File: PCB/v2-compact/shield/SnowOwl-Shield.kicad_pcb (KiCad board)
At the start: 4 copper layers, 60 x 85 mm, 1 part, among them J1 STACK_2x10

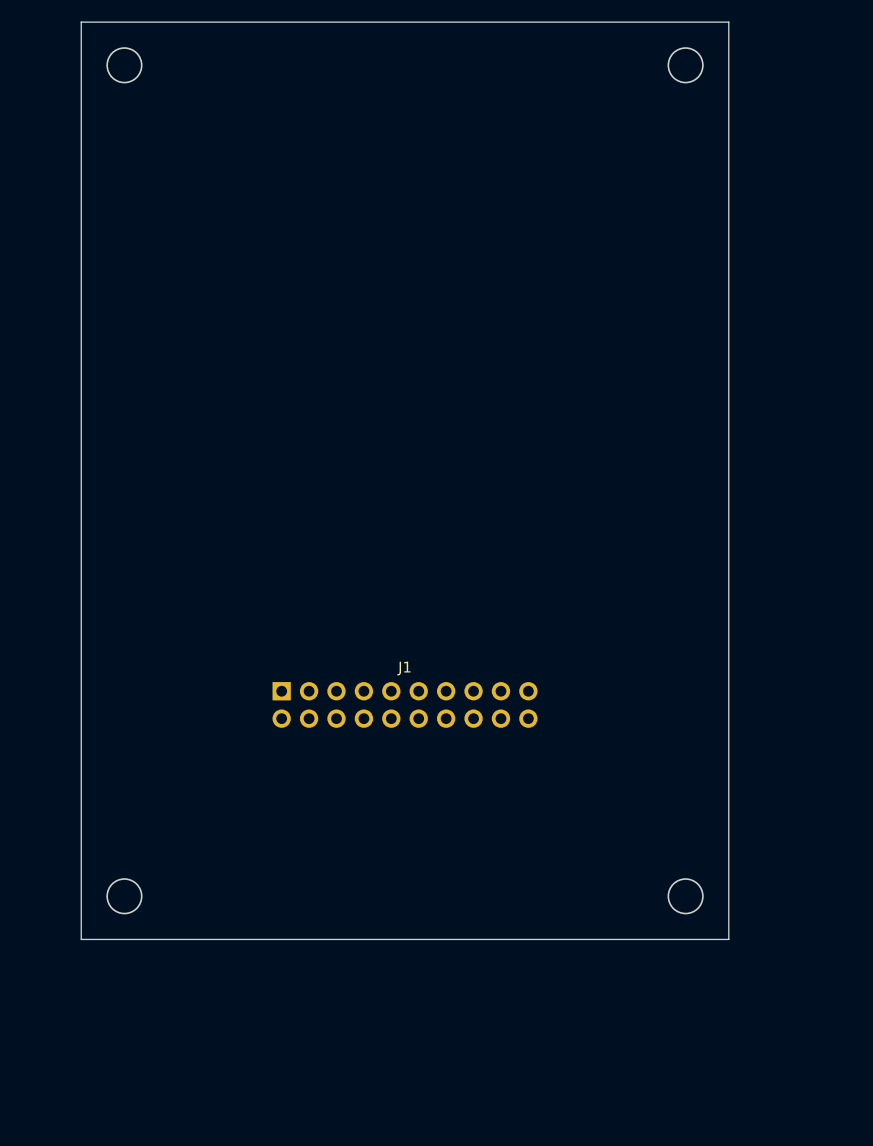
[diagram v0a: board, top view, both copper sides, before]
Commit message: PCB v2: grow to 70x100mm and adopt the C5-owns-radios architecture
Refit the outline to 70x100 after a footprint fit-check: 60x85 could not hold
the RV1106 SoM plus the C5 and nRF24 modules without cramming, which is what
forces congested traces.

- ESP32-C5 now masters the shield SPI spine; every SPI radio taps off it, so
  the whole radio fan-out stays on the shield next to the C5. The S3 commands
  the C5 over one UART on J1 and no SPI radio line crosses the stack header.
- Reflow both boards' zones for short-trace placement, sized to the real part
  footprints; keep the shared J1 datum (53.57, 106.0) so the boards still stack.
- Lock the J1 pinout: power + I2C(PN532) + S3<->C5 UART + S3<->RV1106 UART +
  IR + 1-Wire, with grounds spread for clean returns.
- Rewrite PLACEMENT.md as the updated contract; refresh the shield schematic
  intent note and both floorplan SVGs.
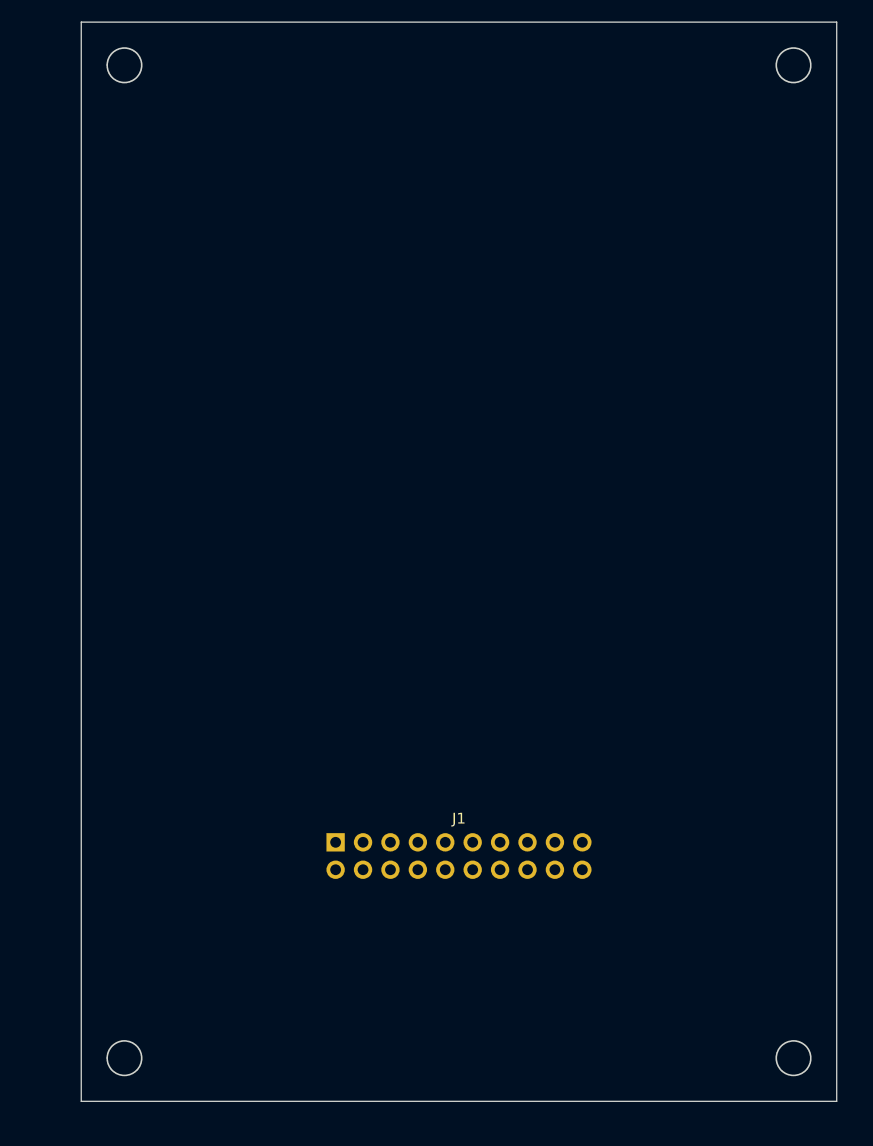
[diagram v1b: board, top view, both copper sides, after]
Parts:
- moved J1 14.9 mm to (53.6, 106.0)
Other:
- board size 60 x 85 mm -> 70 x 100 mm
- board text added: "(BACK) HTRC110 125k + coil"
- board text added: "< LF coil 125k"
- board text added: "< NFC coil 13.56M"
- board text added: "ESP32-C5 (SPI MASTER)"
- board text added: "FRONT=User.1 BACK=User.2 C5 masters shield SPI spine; J1 = power + S3/RV1106 links"
- board text added: "RV1106 USB-C + uSD >"
- board text removed: "(BACK) HTRC110 125kHz + coil"
- board text removed: "< LF coil"
- board text removed: "< NFC coil"
- board text removed: "ESP32-C5 + LDO (U.FL)"
- board text removed: "FRONT zones = User.1 BACK zones = User.2 (floorplan skeleton)"
- board text removed: "RV1106 USB-C >"

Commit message: PCB: import schematic netlists onto both boards (parts placed + nets assigned)
Load every footprint from the schematic into the floorplan-skeleton boards,
place each in its subsystem's zone (grid-spread, back-side sheets flipped), and
assign all nets. Shield: 79 parts, 419 pad-nets, 153 nets. Main: 29 parts,
150 pad-nets, 57 nets. Register the Espressif footprint library; add a
placeholder Core1106 SoM footprint; assign the C5 (Espressif), NEO-M9N (ublox_NEO)
and CC1101 (2x4 header) module footprints.

This is the initial import: every part is on its board with the full ratsnest,
ready for placement refinement and routing.
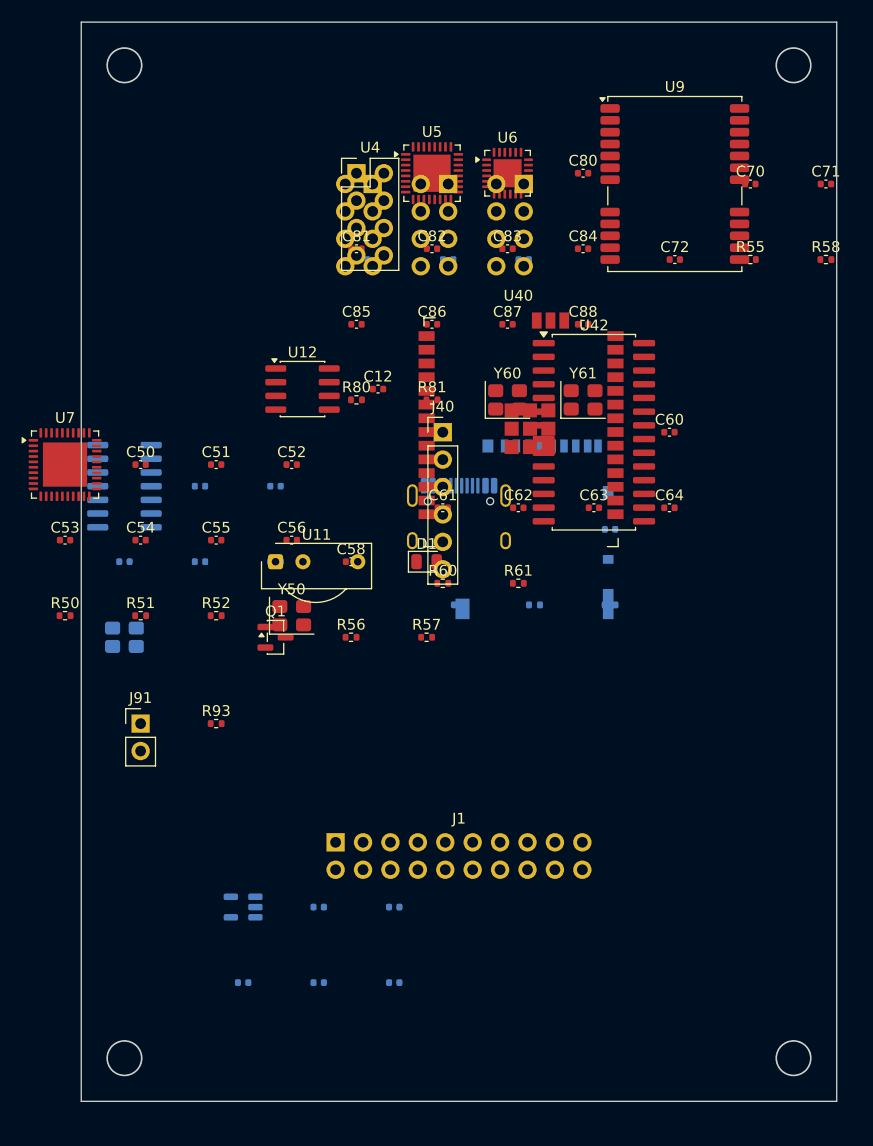
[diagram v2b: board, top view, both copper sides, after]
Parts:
- added C10: 100nF, C_0402_1005Metric, B.Cu at (57.0, 52.0)
- added C12: 100nF, C_0402_1005Metric, F.Cu at (57.5, 64.0)
- added C20: 100nF, C_0402_1005Metric, B.Cu at (64.0, 52.0)
- added C30: 100nF, C_0402_1005Metric, B.Cu at (71.0, 52.0)
- added C40: 10uF, C_0402_1005Metric, B.Cu at (52.0, 112.0)
- added C41: 10uF, C_0402_1005Metric, B.Cu at (59.0, 112.0)
- added C42: 100nF, C_0402_1005Metric, B.Cu at (45.0, 119.0)
- added C43: 22uF, C_0402_1005Metric, B.Cu at (52.0, 119.0)
- added C44: 22uF, C_0402_1005Metric, B.Cu at (59.0, 119.0)
- added C50: 18pF, C_0402_1005Metric, F.Cu at (35.5, 71.0)
- added C51: 18pF, C_0402_1005Metric, F.Cu at (42.5, 71.0)
- added C52: 100nF, C_0402_1005Metric, F.Cu at (49.5, 71.0)
- added C53: 100nF, C_0402_1005Metric, F.Cu at (28.5, 78.0)
- added C54: 1uF, C_0402_1005Metric, F.Cu at (35.5, 78.0)
- added C55: 100nF, C_0402_1005Metric, F.Cu at (42.5, 78.0)
- added C56: 100nF, C_0402_1005Metric, F.Cu at (49.5, 78.0)
- added C58: 100nF, C_0402_1005Metric, F.Cu at (55.0, 80.0)
- added C60: 10uF, C_0402_1005Metric, F.Cu at (84.5, 68.0)
- added C61: 100nF, C_0402_1005Metric, F.Cu at (63.5, 75.0)
- added C62: 100nF, C_0402_1005Metric, F.Cu at (70.5, 75.0)
- added C63: 1uF, C_0402_1005Metric, F.Cu at (77.5, 75.0)
- added C64: 100nF, C_0402_1005Metric, F.Cu at (84.5, 75.0)
- added C70: 100nF, C_0402_1005Metric, F.Cu at (92.0, 45.0)
- added C71: 10uF, C_0402_1005Metric, F.Cu at (99.0, 45.0)
- added C72: 1uF, C_0402_1005Metric, F.Cu at (85.0, 52.0)
- added C80: 10pF, C_0402_1005Metric, F.Cu at (76.5, 44.0)
- added C81: 10pF, C_0402_1005Metric, F.Cu at (55.5, 51.0)
- added C82: 100nF, C_0402_1005Metric, F.Cu at (62.5, 51.0)
- added C83: 100nF, C_0402_1005Metric, F.Cu at (69.5, 51.0)
- added C84: 12pF, C_0402_1005Metric, F.Cu at (76.5, 51.0)
- added C85: 12pF, C_0402_1005Metric, F.Cu at (55.5, 58.0)
- added C86: 100nF, C_0402_1005Metric, F.Cu at (62.5, 58.0)
- added C87: 100nF, C_0402_1005Metric, F.Cu at (69.5, 58.0)
- added C88: 100nF, C_0402_1005Metric, F.Cu at (76.5, 58.0)
- added C90: 18pF, C_0402_1005Metric, B.Cu at (41.0, 73.0)
- added C91: 18pF, C_0402_1005Metric, B.Cu at (48.0, 73.0)
- added C92: 100nF, C_0402_1005Metric, B.Cu at (34.0, 80.0)
- added C93: 10uF, C_0402_1005Metric, B.Cu at (41.0, 80.0)
- added C94: 10uF, C_0402_1005Metric, B.Cu at (79.0, 77.0)
- added C95: 10uF, C_0402_1005Metric, B.Cu at (65.0, 84.0)
- added D1: IR_LED, LED_0805_2012Metric, F.Cu at (62.0, 80.0)
- added J40: C5_PROG_UART, PinHeader_1x06_P2.54mm_Vertical, F.Cu at (63.5, 68.0)
- added J50: USB-C, USB_C_Receptacle_HRO_TYPE-C-31-M-12, B.Cu at (65.0, 77.0)
- added J51: microSD, microSD_HC_Hirose_DM3AT-SF-PEJM5, B.Cu at (72.0, 77.0)
- added J91: iButton, PinHeader_1x02_P2.54mm_Vertical, F.Cu at (35.5, 95.0)
- added Q1: MMBT3904, SOT-23, F.Cu at (48.0, 87.0)
- added R50: 4k7, R_0402_1005Metric, F.Cu at (28.5, 85.0)
- added R51: 4k7, R_0402_1005Metric, F.Cu at (35.5, 85.0)
- added R52: 10k, R_0402_1005Metric, F.Cu at (42.5, 85.0)
- added R55: 0R, R_0402_1005Metric, F.Cu at (92.0, 52.0)
- added R56: 33R, R_0402_1005Metric, F.Cu at (55.0, 87.0)
- added R57: 220R, R_0402_1005Metric, F.Cu at (62.0, 87.0)
- added R58: 10k, R_0402_1005Metric, F.Cu at (99.0, 52.0)
- added R60: 10k, R_0402_1005Metric, F.Cu at (63.5, 82.0)
- added R61: 10k, R_0402_1005Metric, F.Cu at (70.5, 82.0)
- added R80: 56k, R_0402_1005Metric, F.Cu at (55.5, 65.0)
- added R81: 10k, R_0402_1005Metric, F.Cu at (62.5, 65.0)
- added R90: 10k, R_0402_1005Metric, B.Cu at (48.0, 80.0)
- added R93: 4k7, R_0402_1005Metric, F.Cu at (42.5, 95.0)
- added R95: 5k1, R_0402_1005Metric, B.Cu at (72.0, 84.0)
- added R96: 5k1, R_0402_1005Metric, B.Cu at (79.0, 84.0)
- added U1: nRF24L01+, PinHeader_2x04_P2.54mm_Vertical, B.Cu at (57.0, 45.0)
- added U11: TSOP38238, Vishay_CAST-3Pin, F.Cu at (48.0, 80.0)
- added U12: W25Q128JVSSIQ, SOIC-8_3.9x4.9mm_P1.27mm, F.Cu at (50.5, 64.0)
- added U2: nRF24L01+, PinHeader_2x04_P2.54mm_Vertical, B.Cu at (64.0, 45.0)
- added U3: nRF24L01+, PinHeader_2x04_P2.54mm_Vertical, B.Cu at (71.0, 45.0)
- added U4: CC1101, PinHeader_2x04_P2.54mm_Vertical, F.Cu at (55.5, 44.0)
- added U40: ESP32-C5-WROOM-1U-N16R4, ESP32-C5-WROOM-1U, F.Cu at (70.5, 68.0)
- added U41: AP7361C-3.3, SOT-23-5, B.Cu at (45.0, 112.0)
- added U42: MCP23S17, SOIC-28W_7.5x17.9mm_P1.27mm, F.Cu at (77.5, 68.0)
- added U5: CC1200RHBR, QFN-32-1EP_5x5mm_P0.5mm_EP3.45x3.45mm, F.Cu at (62.5, 44.0)
- added U6: SX1262IMLTRT, QFN-24-1EP_4x4mm_P0.5mm_EP2.6x2.6mm, F.Cu at (69.5, 44.0)
- added U7: PN532, HVQFN-40-1EP_6x6mm_P0.5mm_EP4.1x4.1mm, F.Cu at (28.5, 71.0)
- added U8: HTRC11001T, SOIC-14_3.9x8.7mm_P1.27mm, B.Cu at (34.0, 73.0)
- added U9: NEO-M9N, ublox_NEO, F.Cu at (85.0, 45.0)
- added Y50: 27.12MHz, Crystal_SMD_3225-4Pin_3.2x2.5mm, F.Cu at (49.5, 85.0)
- added Y60: 40MHz, Crystal_SMD_3225-4Pin_3.2x2.5mm, F.Cu at (69.5, 65.0)
- added Y61: 32MHz, Crystal_SMD_3225-4Pin_3.2x2.5mm, F.Cu at (76.5, 65.0)
- added Y90: 4MHz, Crystal_SMD_3225-4Pin_3.2x2.5mm, B.Cu at (34.0, 87.0)
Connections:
- J1 pad 1: (no net) -> +5V
- J1 pad 10: (no net) -> CC12_DCPL
- J1 pad 11: (no net) -> CC12_DCPL
- J1 pad 12: (no net) -> OW_1WIRE
- J1 pad 13: (no net) -> IR_RX
- J1 pad 14: (no net) -> IR_TX
- J1 pad 15: (no net) -> CC12_DCPL
- J1 pad 16: (no net) -> RV_TX
- J1 pad 17: (no net) -> RV_RX
- J1 pad 18: (no net) -> RV_CTRL
- J1 pad 19: (no net) -> SPARE
- J1 pad 2: (no net) -> +3V3
- J1 pad 20: (no net) -> CC12_DCPL
- J1 pad 3: (no net) -> CC12_DCPL
- J1 pad 4: (no net) -> SDA
- J1 pad 5: (no net) -> SCL
- J1 pad 6: (no net) -> CC12_DCPL
- J1 pad 7: (no net) -> C5_TX
- J1 pad 8: (no net) -> C5_RX
- J1 pad 9: (no net) -> C5_DRDY

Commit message: PCB: intentional floorplan placement + 3D models + screen (both boards)
Reflow both boards to the PLACEMENT.md contract instead of a mechanical grid:
- Shield: radios north each behind its SMA, C5 (SPI master) centre with U.FL, the
  3 nRF24 on the back behind the QFN radios, MCP expander on the spine, PN532/flash/
  IR/iButton in their zones, J1 at the (53.57,106) datum, prog header off the crowded
  east edge. Main: pure-UI front (status LEDs, landscape TFT area, PlayStation D-pad
  SW1 up/SW2 down/SW3 left/SW4 right + SW5 select, J1 datum), all electronics on the
  back (S3 upper-centre with antenna to the edge, microSD east, power+USB-C south).
- Every support part anchored to the exact pin it shares a net with, then de-overlapped
  by spiralling out to the nearest clear spot inside the board, so decoupling hugs the
  power pins and crystals sit at the XTAL pins.
- Verified: 0 same-side courtyard overlaps, 0 cross-side through-hole collisions (new
  check that caught headers landing on back-side modules), every part in the outline.
- 3D models the renderer can find: C5 repointed to the Espressif model's absolute path,
  J1 given the KiCad 2x10 header body (rotated to match the horizontal pad layout).
- Draw the TFT display outline + label on the main front so the screen is visible.

Note: U9 (u-blox NEO) still renders as an outline - RF_GPS.3dshapes is absent from this
KiCad 3D pack; the footprint/courtyard are correct, only the cosmetic .step is missing.
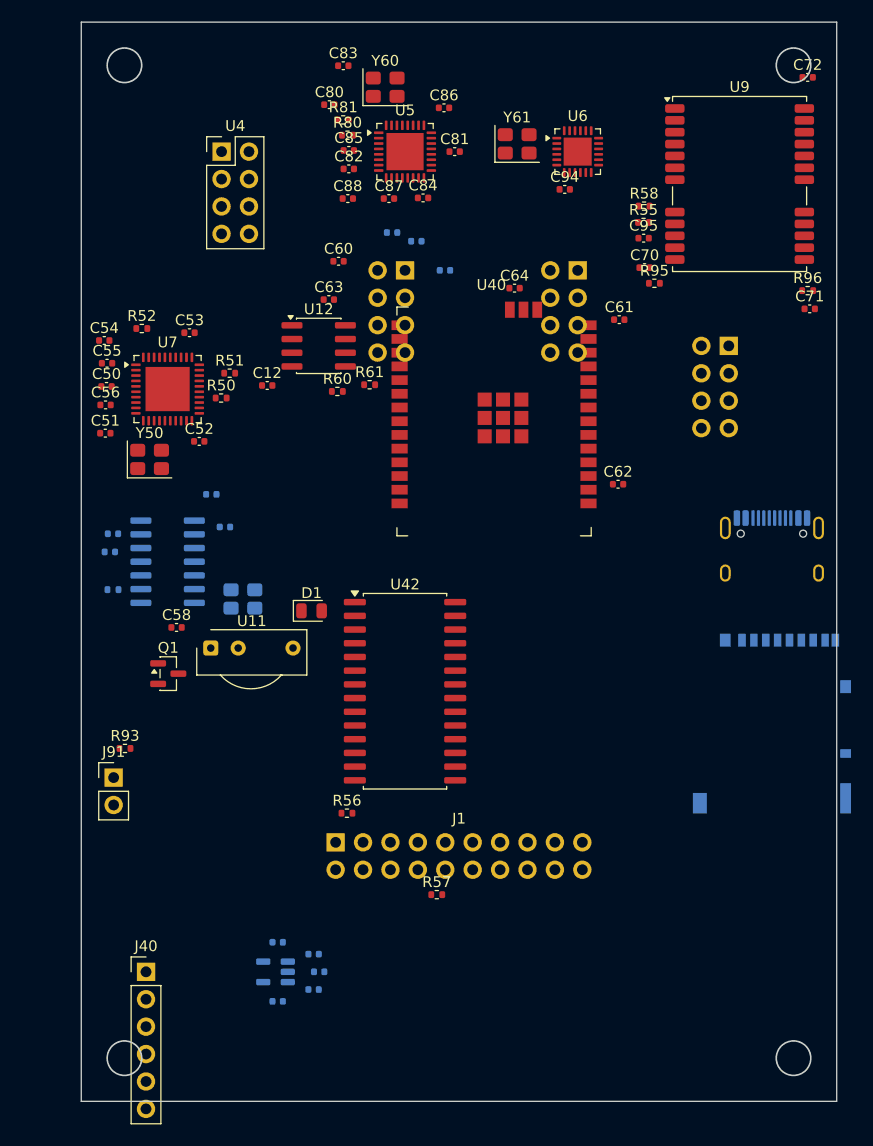
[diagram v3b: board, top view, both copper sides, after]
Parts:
- C94, C95, R95, R96: moved to F.Cu
- moved J40 57.1 mm to (36.0, 118.0)
- moved C95 38.0 mm to (82.1, 50.0), turned to 0 degrees
- moved C60 34.5 mm to (53.8, 52.2)
- moved R96 34.4 mm to (97.3, 54.9), turned to 0 degrees
- moved R95 31.8 mm to (83.1, 54.2), turned to 0 degrees
- moved C94 31.8 mm to (74.8, 45.5), turned to 0 degrees
- moved C63 31.2 mm to (52.9, 55.7)
- moved Y60 31.1 mm to (58.2, 36.0)
- moved U42 29.7 mm to (60.0, 92.0)
- moved J50 29.2 mm to (94.0, 80.0)
- moved J51 28.4 mm to (94.0, 95.0)
- moved R52 27.5 mm to (35.6, 58.4)
- moved R81 27.2 mm to (54.3, 39.1)
- moved C64 24.9 mm to (70.2, 54.6)
- moved R50 24.8 mm to (43.0, 64.8)
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
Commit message: PCB: clear mounting-hole keepouts, pull off-board parts in, fix missing models
Second verification pass with a new thorough checker (mounting-hole clearance +
3D-model-FILE-exists, not just referenced):
- Mounting holes: add an M3 screw-head/standoff keepout to the placement engine so
  no support part lands near a corner hole (was dropping caps like C72 onto them).
  Move the parts that sat on holes: shield U9/U6 reflowed in the NE, prog header J40
  off the bottom-left hole; main S3 nudged clear of the NW hole.
- Off-board: J40 was hanging 4.5mm off the bottom edge (origin at pin 1) and J51 1.8mm
  off the east edge - both pulled fully inside the outline.
- Missing 3D model files (referenced but absent from this KiCad 3D pack): repoint U7's
  PN532 to the near-identical QFN-40 6x6 model, and the USB-C receptacles (J50/J20) to
  a GCT USB-C body, both present on disk.
- Result on both boards: 0 same-side overlaps, 0 cross-side hole collisions, 0 parts
  too close to a mounting hole, nothing hanging off the outline.

Still outstanding: only U9 (u-blox NEO) lacks a 3D model - RF_GPS.3dshapes is entirely
absent from this install's 3D pack (footprint/courtyard correct; needs the 3D pack).
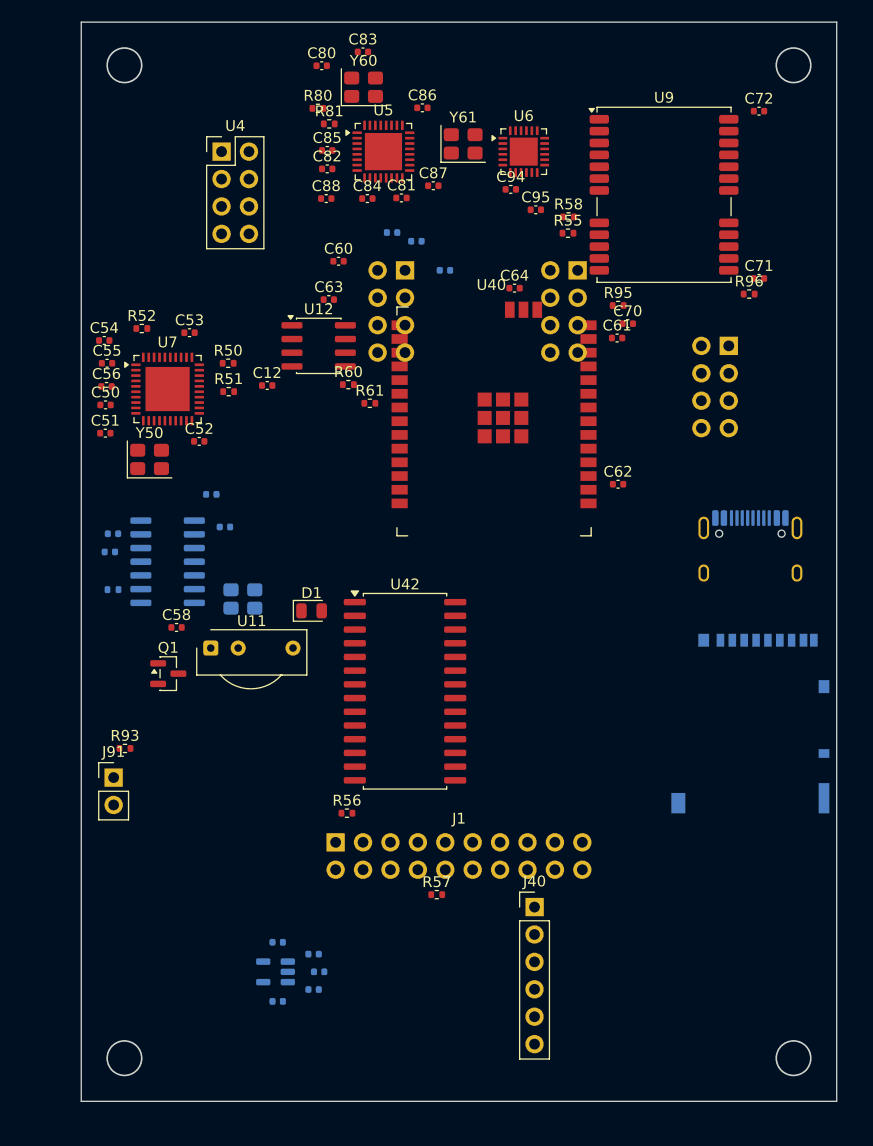
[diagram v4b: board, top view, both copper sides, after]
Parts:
- moved J40 36.5 mm to (72.0, 112.0)
- moved C95 10.3 mm to (72.1, 47.4)
- moved R55 7.07 mm to (75.1, 49.6)
- moved R58 7.07 mm to (75.2, 48.0)
- moved U9 7.07 mm to (84.0, 46.0)
- moved C81 6.54 mm to (59.7, 46.3)
- moved C72 5.49 mm to (92.8, 38.2)
- moved C71 5.48 mm to (92.8, 53.8)
- moved R96 5.43 mm to (91.9, 55.2)
- moved C70 5.42 mm to (80.6, 57.9)
- moved C84 5.16 mm to (56.5, 46.4)
- moved C94 5.00 mm to (69.8, 45.5)
- moved U6 5.00 mm to (71.0, 42.0)
- moved Y61 5.00 mm to (65.4, 41.3)
- moved C87 4.28 mm to (62.6, 45.2)
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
